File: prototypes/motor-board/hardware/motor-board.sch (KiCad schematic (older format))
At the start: 32 parts, among them J1 PJ-063AH, J2 Conn_01x02, J3 PinHeader_01x06, U1 TLV70245_SOT23-5, U2 TB67H450FNG, U3 TLV9051, U4 LMV331, U5 TCST1202

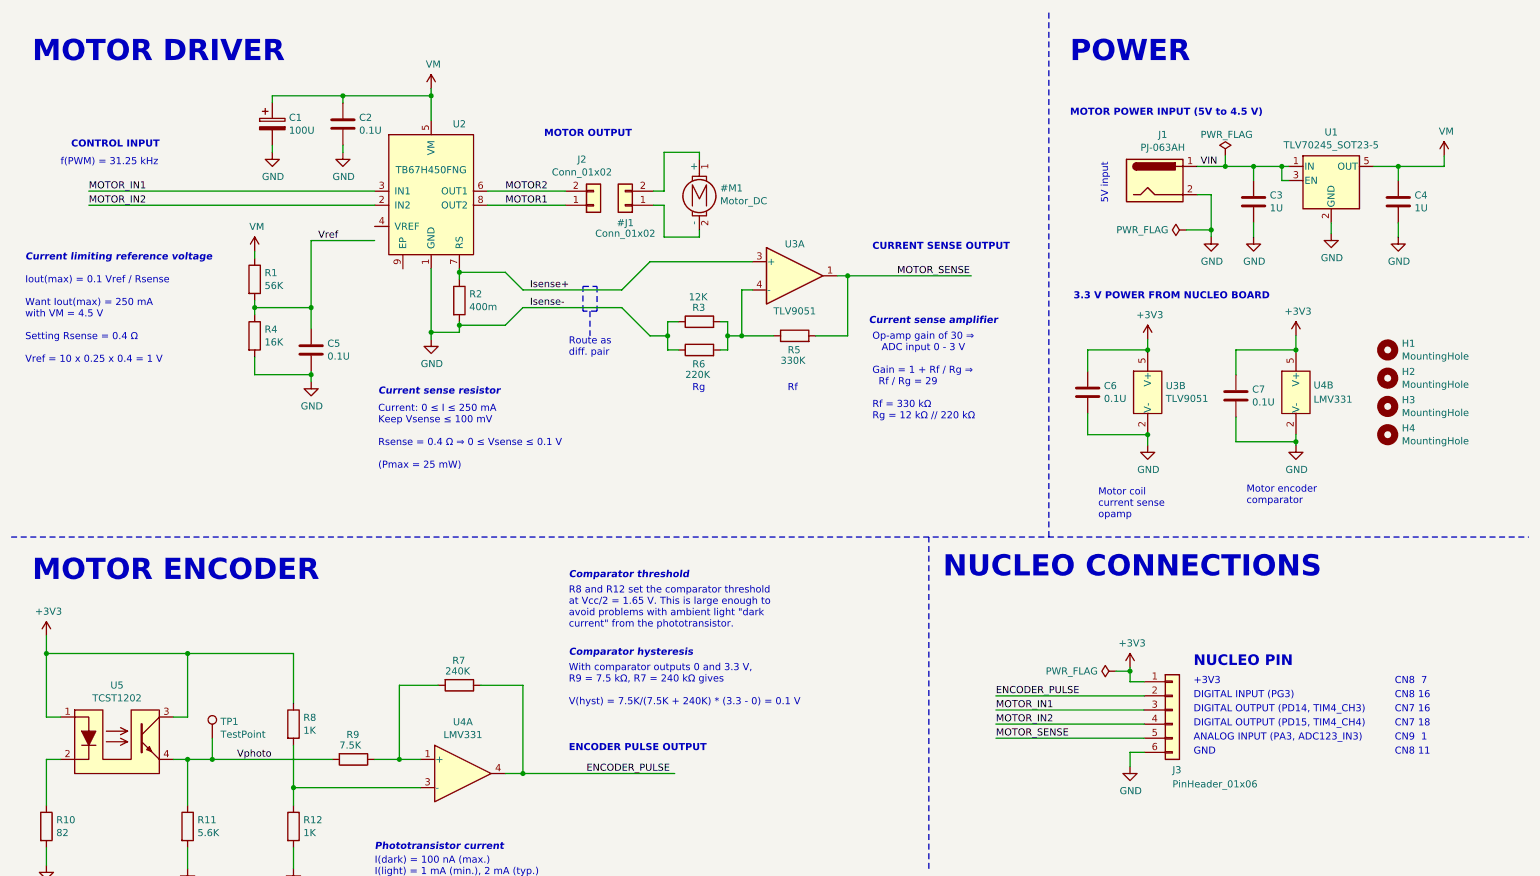
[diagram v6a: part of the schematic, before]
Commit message: Finalise motor board layout; schematic and layout checklist
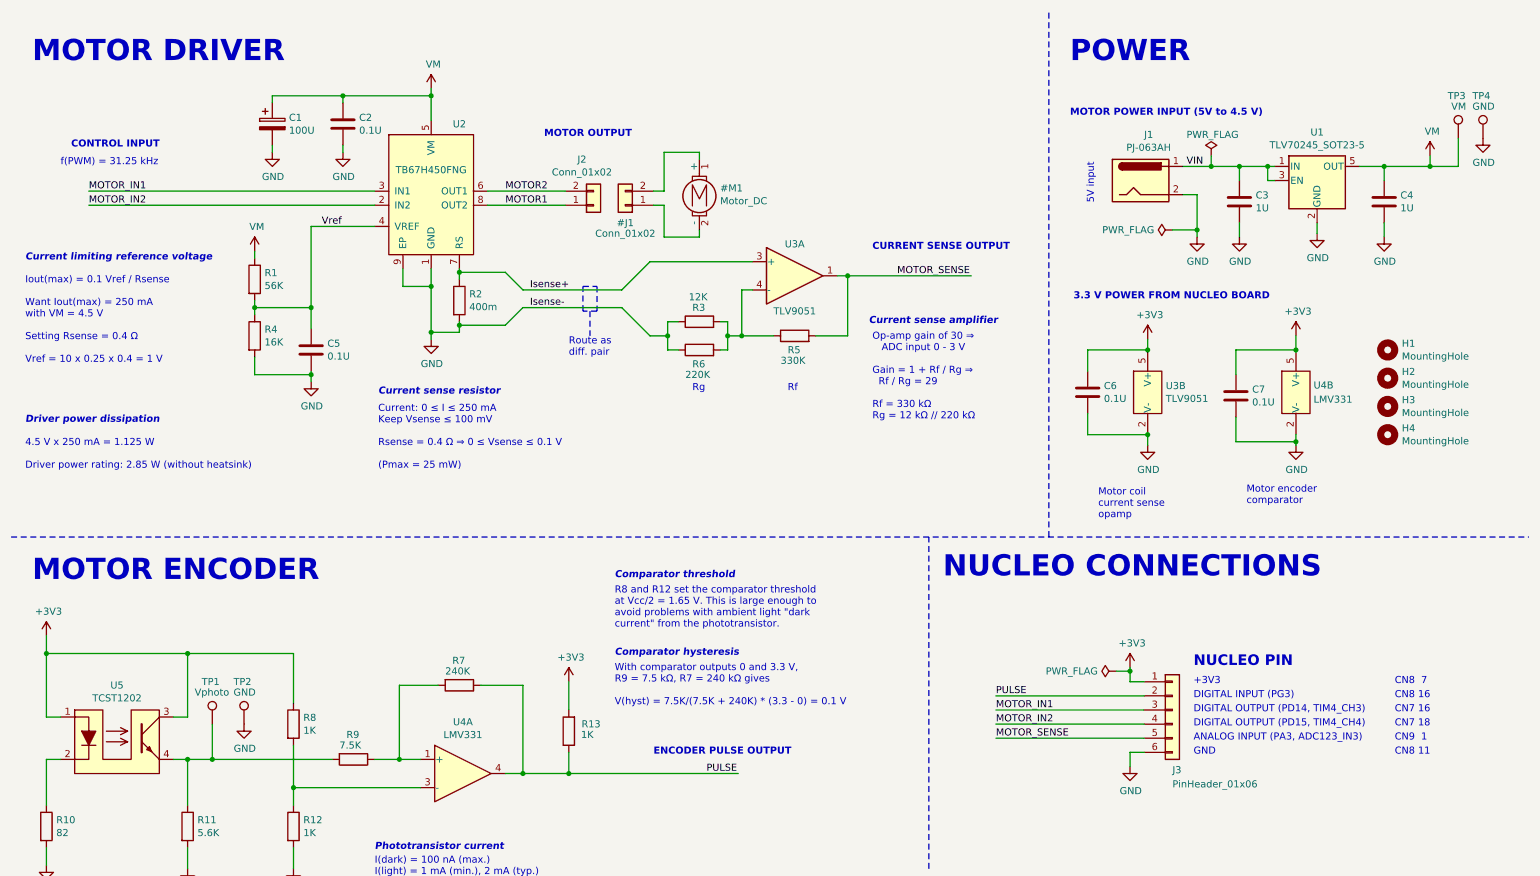
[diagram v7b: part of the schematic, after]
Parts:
- added R13: 1K, mini-mapper:R_0805, symbol mini-mapper:R
- added TP2, TP4: GND, mini-mapper:TestPoint_Pad_2.0x2.0mm, symbol mini-mapper:TestPoint
- added TP3: VM, mini-mapper:TestPoint_Pad_2.0x2.0mm, symbol mini-mapper:TestPoint
- TP1: value TestPoint -> Vphoto
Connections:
- net +3V3: now also R13.2
- net GND: now also U2.9 (EP), TP2.1, TP4.1
- net VM: now also TP3.1
- net Vref: now also U2.4 (VREF)
- net ENCODER_PULSE renamed PULSE
- net PULSE: now also R13.1
- net Vphoto: no longer names the net of R11.1, R9.2, TP1.1, U5.4
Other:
- note added: "4.5 V x 250 mA = 1.125 W\n\nDriver power rating: 2.85 W (without heatsink)"
- note added: "Driver power dissipation"
- moved on the sheet: C3, C4, J1, TP1, U1
